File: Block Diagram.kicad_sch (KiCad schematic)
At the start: 0 parts

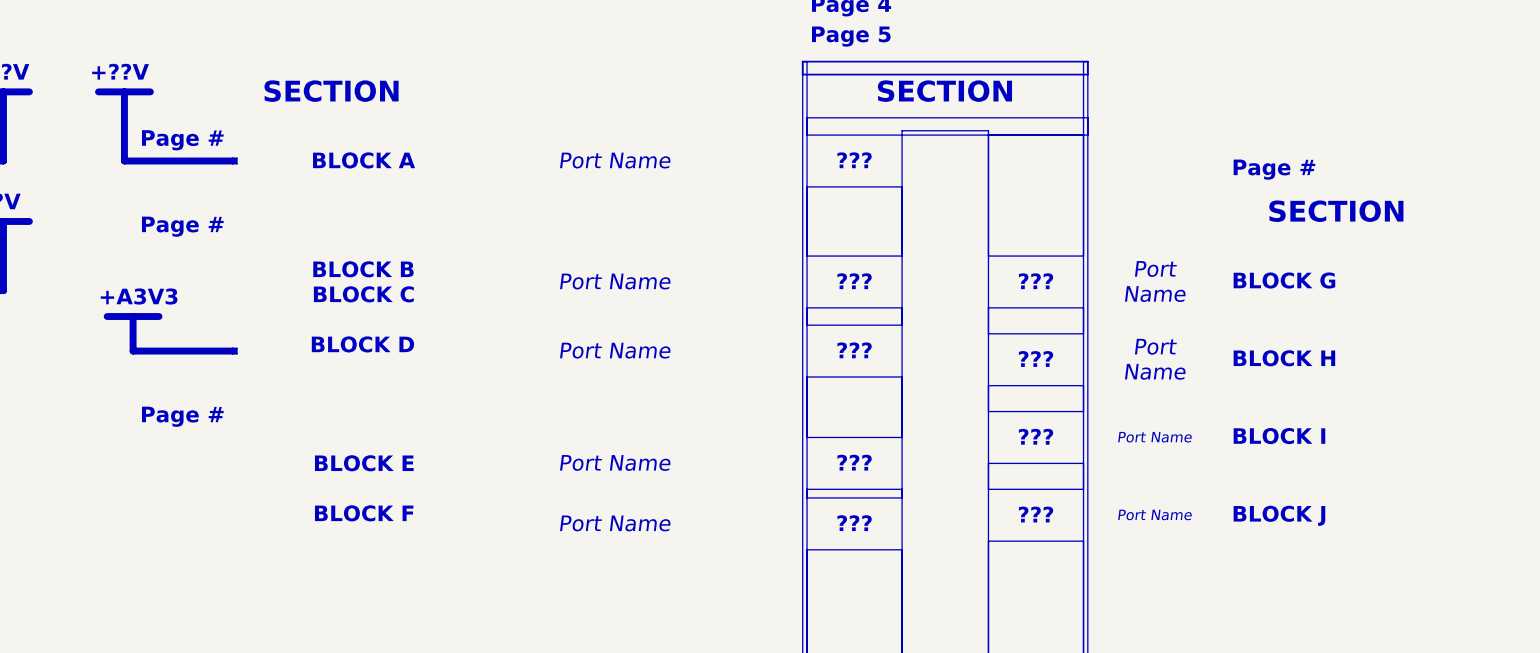
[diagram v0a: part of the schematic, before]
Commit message: Added conformal coat generation, removed KiRi to prevent bloat and dropped the power sequencing sheet
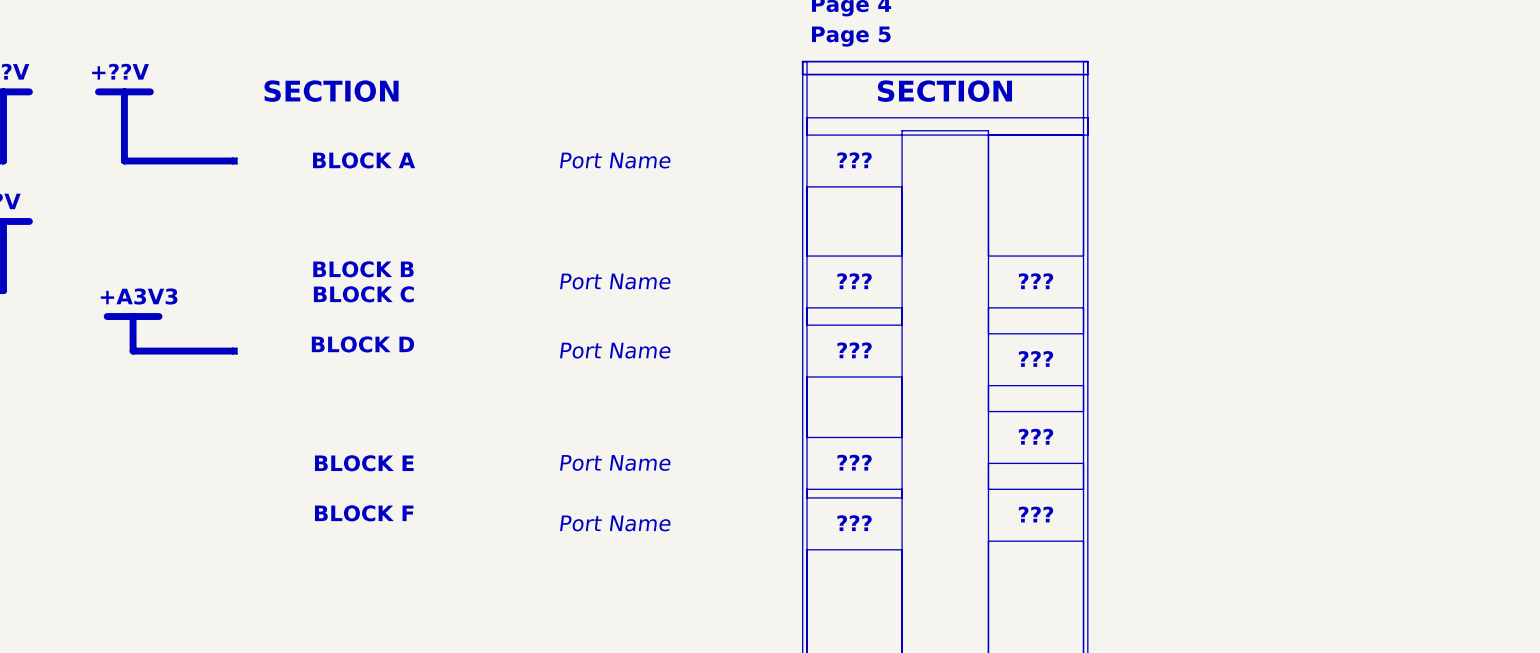
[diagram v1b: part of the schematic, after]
